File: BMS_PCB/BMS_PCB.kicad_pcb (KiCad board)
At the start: 2 copper layers, 168 parts, among them IC1 TPS560430XFDBVT, IC3 AMC1350DWVR, IC4 AMC1350DWVR, IC5 AMC1350DWVR, IC6 AMC1350DWVR, J1 Conn_01x37, J2 Conn_01x15, K1 J1021AS35VDC.20, Q1 2N7002KT7G, U1 TLV2404IDR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

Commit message: Bugfix Leiterbahn
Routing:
- net Net-(U3B--): track 28.5 -> 25.7 mm
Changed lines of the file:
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@@
-	)
-	(segment
-		(start 71.829501 136.4105)
-		(end 68.786503 136.4105)
-		(width 0.2)
-		(layer "F.Cu")
-		(net 31)
 	)
 	(segment
@@
 	)
 	(segment
-		(start 78.798 136.4105)
-		(end 64.779501 136.4105)
+		(start 64.421251 136.76875)
+		(end 61.516001 139.674)
 		(width 0.2)
 		(layer "F.Cu")
@@
 	)
 	(segment
-		(start 64.779501 136.4105)
-		(end 61.516001 139.674)
+		(start 79.15625 136.76875)
+		(end 79.15625 137.14375)
 		(width 0.2)
 		(layer "F.Cu")
@@
 	(segment
 		(start 79.15625 136.76875)
-		(end 79.15625 137.14375)
+		(end 64.421251 136.76875)
 		(width 0.2)
 		(layer "F.Cu")

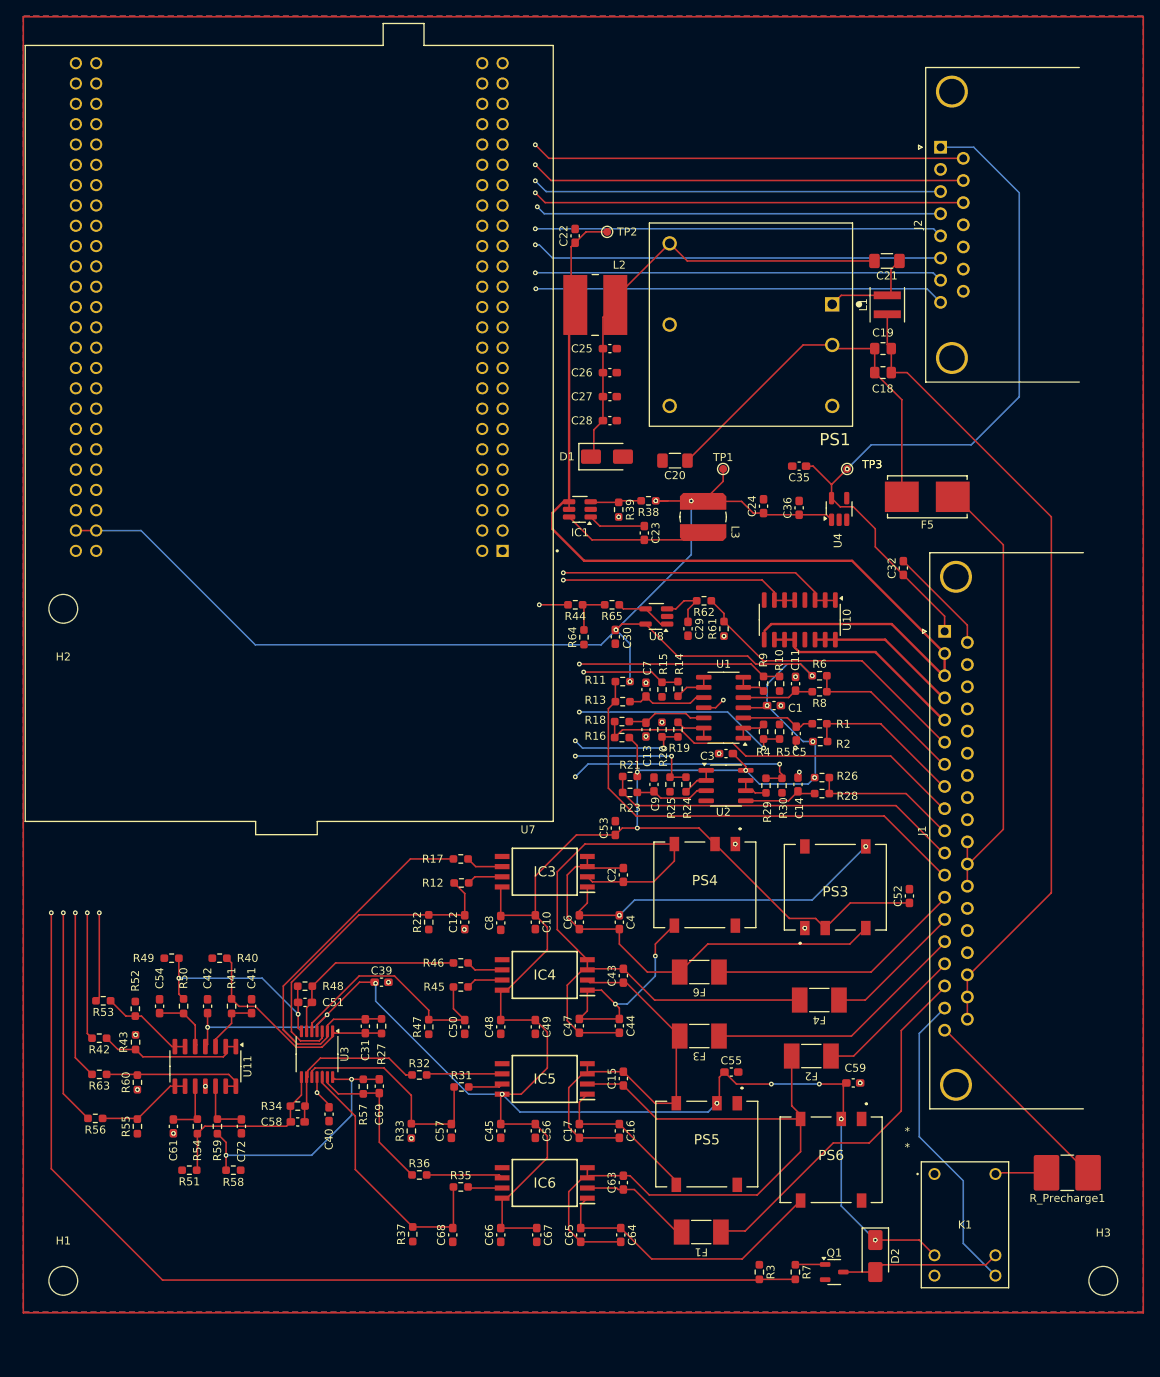
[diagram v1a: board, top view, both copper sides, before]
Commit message: Edge Cut hinzugefügt
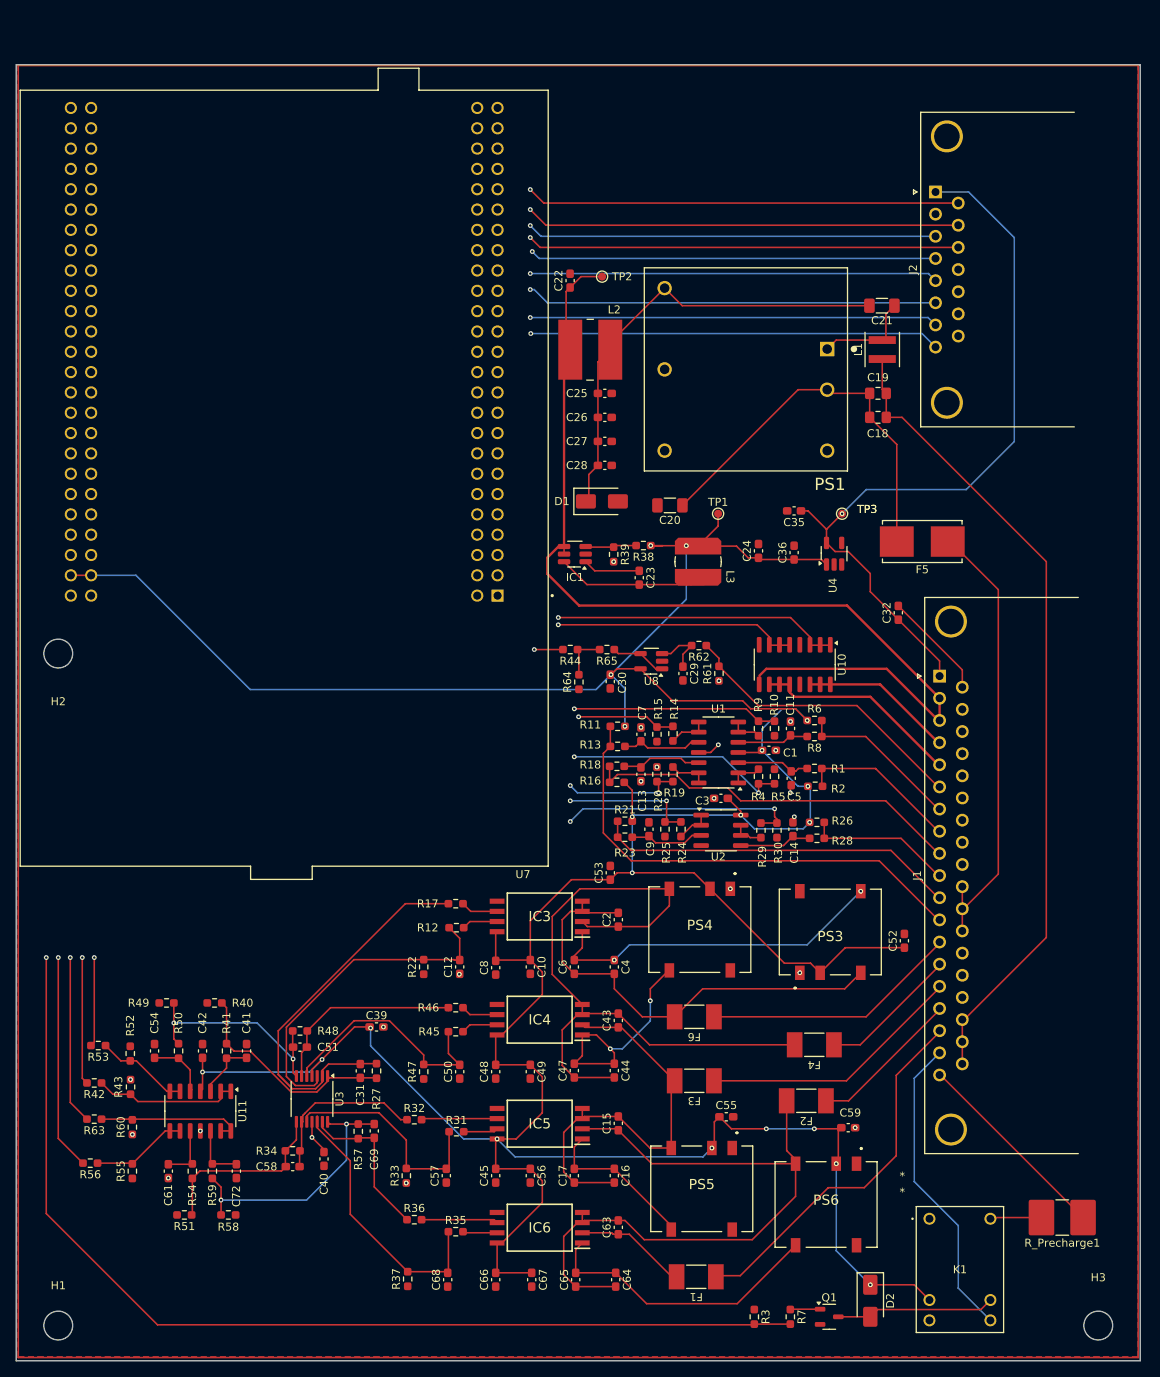
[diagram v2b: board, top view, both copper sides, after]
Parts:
- moved C2 5.63 mm to (99.8, 131.4)
- moved IC3 5.63 mm to (89.9, 131.0)
- moved R12 5.63 mm to (79.5, 132.4)
- moved R17 5.63 mm to (79.4, 129.4)
- moved C25 5.63 mm to (98.1, 65.6)
- moved C26 5.63 mm to (98.1, 68.6)
- moved C32 5.63 mm to (134.8, 93.0)
- moved D2 5.63 mm to (131.3, 179.0)
- moved C11 5.63 mm to (121.3, 107.5)
- moved C22 5.63 mm to (93.7, 51.5)
- moved C23 5.63 mm to (102.4, 88.6)
- moved C24 5.63 mm to (117.3, 85.3)
- moved C30 5.63 mm to (98.8, 101.6)
- moved C35 5.63 mm to (121.7, 80.3)
- moved C36 5.63 mm to (121.7, 85.5)
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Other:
- board outline added: 140.5 x 162 mm

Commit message: few changes
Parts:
- removed C32: 0,1uF, Capacitor_SMD:C_0603_1608Metric_Pad1.08x0.95mm_HandSolder
- removed H1, H2, H3: MountingHole_3.6mm, MountingHole:MountingHole_3.7mm
- added C33: 0,1uF, Resistor_SMD:R_0603_1608Metric_Pad0.98x0.95mm_HandSolder, F.Cu at (132.9, 91.0)
- C52, C53, C55, C59: footprint Capacitor_SMD:C_0603_1608Metric_Pad1.08x0.95mm_HandSolder -> Resistor_SMD:R_1206_3216Metric_Pad1.30x1.75mm_HandSolder
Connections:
- net Display_CLK renamed Display_SCK
- net Vcc_Current renamed +3.3V
- C22 pad 1: Relais_in+ -> +12V
- IC1 pad 4: Relais_in+ -> +12V
- IC1 pad 5: Relais_in+ -> +12V
- J1 pad 2: Relais_in+ -> Relais_in-
- J1 pad 4: Relais_out+ -> +12V
- J1 pad 5: Relais_out- -> +12V
- J2 pad 6: Display_D/C -> Display_DC
- K1 pad 1: (no net) -> unconnected-(K1-Pad1)
- L2 pad 2: Relais_in+ -> +12V
- TP2 pad 1: Relais_in+ -> +12V
- U10 pad 1: Relais_uC -> Relais+_uC
- U10 pad 10: Relais_out- -> Relais_in-
- U10 pad 11: Relais_out- -> Relais_in-
- U10 pad 12: Relais_out- -> Relais_in-
- U10 pad 14: Relais_out+ -> Relais_in+
- U10 pad 15: Relais_out+ -> Relais_in+
- U10 pad 16: Relais_out+ -> Relais_in+
- U10 pad 2: Relais_uC -> Relais+_uC
- U10 pad 3: Relais_uC -> Relais+_uC
- U10 pad 5: Relais_uC -> Relais-_uC
- U10 pad 6: Relais_uC -> Relais-_uC
- U10 pad 7: Relais_uC -> Relais-_uC
- U10 pad 9: Relais_in+ -> +12V
- U7 pad P1_10: Temp4_uC -> Touchdisplay_x
- U7 pad P1_11: Voltage01_uC -> Current_uC
- U7 pad P1_13: Voltage23_uC -> Voltage12_uC
- U7 pad P1_14: Voltage12_uC -> Voltage01_uC
- U7 pad P1_16: Temp6_uC -> Voltage23_uC
- U7 pad P1_17: Display_MOSI -> Temp1_uC
- U7 pad P1_18: Touchdisplay_x -> Voltage34_uC
- U7 pad P1_19: Temp3_uC -> Temp6_uC
- U7 pad P1_20: Voltage34_uC -> Temp5_uC
- U7 pad P1_21: Temp2_uC -> Temp3_uC
- U7 pad P1_22: Temp1_uC -> Temp2_uC
- U7 pad P1_7: Current_uC -> Temp4_uC
- U7 pad P1_8: Touchdisplay_y -> unconnected-(U7A-PC0-PadP1_8)
- U7 pad P1_9: Temp5_uC -> Touchdisplay_y
- U7 pad P2_23: Display_CS -> unconnected-(U7B-PB6-PadP2_23)
- U7 pad P2_24: Display_D/C -> unconnected-(U7B-PB7-PadP2_24)
- U7 pad P2_26: unconnected-(U7B-PB5-PadP2_26) -> Display_MOSI
- U7 pad P2_27: unconnected-(U7B-PD7-PadP2_27) -> Display_DC
- U7 pad P2_30: unconnected-(U7B-PD6-PadP2_30) -> Display_CS
- U7 pad P2_31: unconnected-(U7B-PD3-PadP2_31) -> Display_RST
- U7 pad P2_33: Relais_uC -> Relais+_uC
- U7 pad P2_34: Display_RST -> Relais-_uC
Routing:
- net Relais_uC: track 66.5 -> 0.00 mm, vias 2 -> 0
- net Display_D/C: track 51.3 -> 0.00 mm, vias 1 -> 0
- net Display_DC: track 0.00 -> 51.3 mm
- net Relais+_uC: track 0.00 -> 36.0 mm, vias 0 -> 1
- net Relais-_uC: track 0.00 -> 30.5 mm, vias 0 -> 1
- net Relais_out-: track 26.4 -> 0.00 mm
- net (no net): track 0.00 -> 26.4 mm
- net Relais_in+: track 127.6 -> 147.2 mm
- net Relais_out+: track 19.6 -> 0.00 mm
- net unconnected-(U7B-PB7-PadP2_24): vias 0 -> 1

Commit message: Freilaufdiode
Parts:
- added D3: 1N4007, Diode_SMD:D_SMA, F.Cu at (113.0, 29.4)
- added D4: 1N4007, Diode_SMD:D_SMA, F.Cu at (113.0, 34.0)
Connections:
- J1 pad 3: Relais_in+ -> +12V
- J1 pad 4: +12V -> Relais_in+

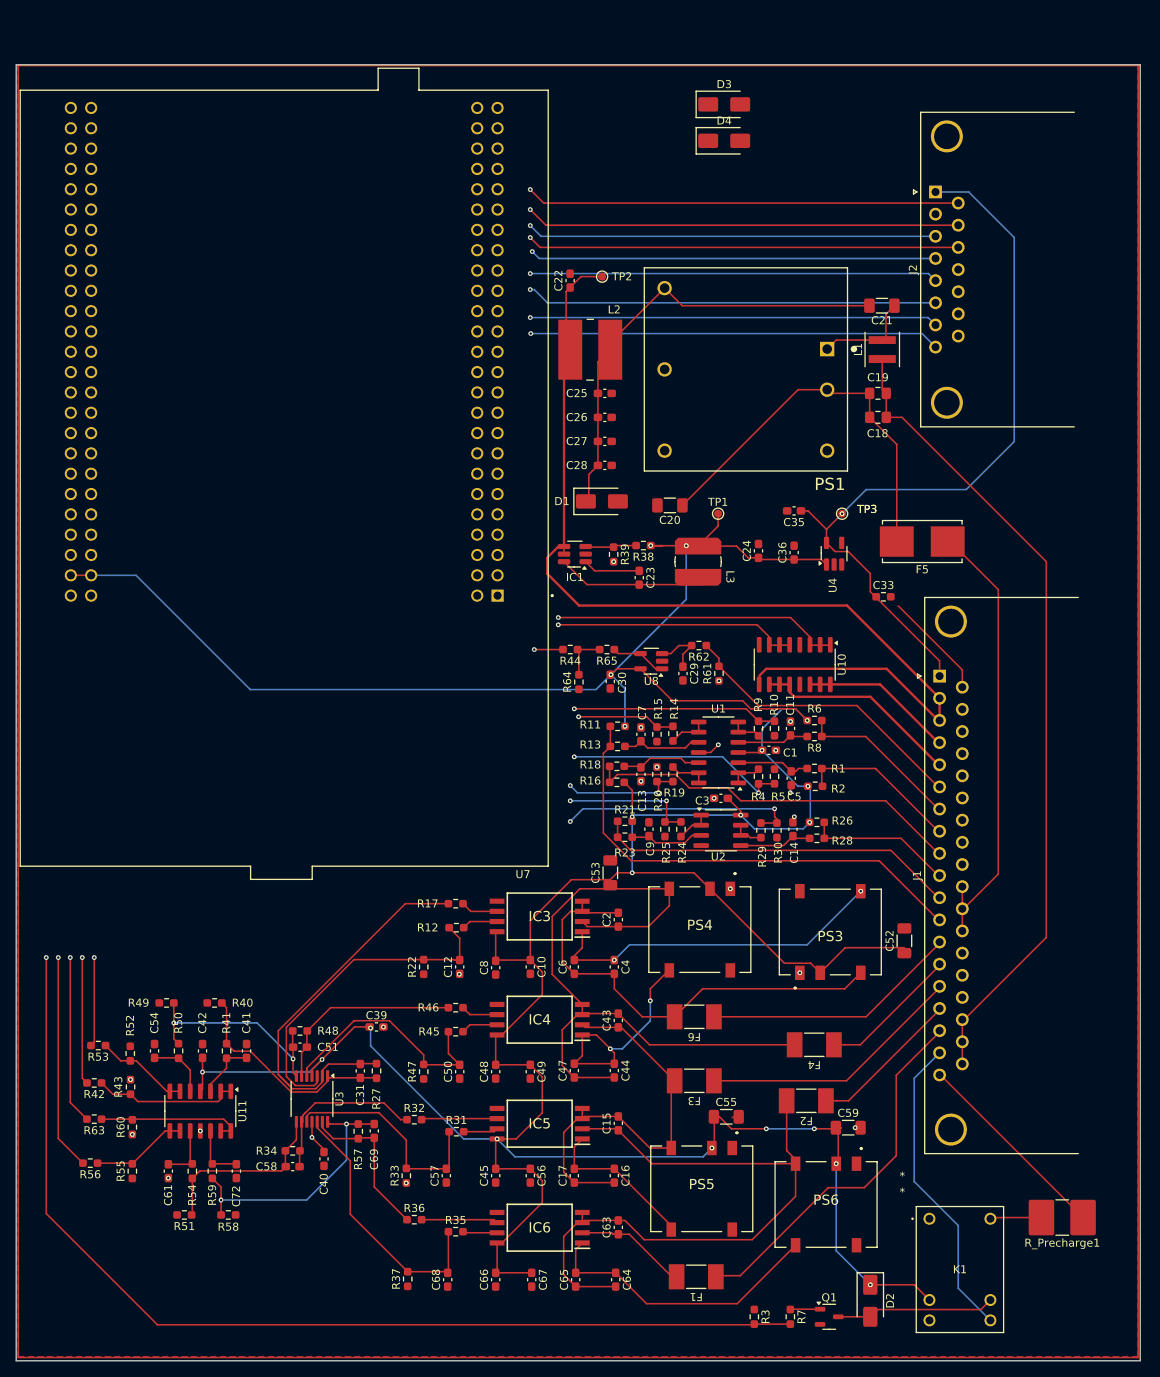
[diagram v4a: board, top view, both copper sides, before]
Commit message: Sonntag, 04.05.
Leiterbahndicken angepasst, Bohrlöcher erneuert, µC final angeschlossen, letzte Bugfixes
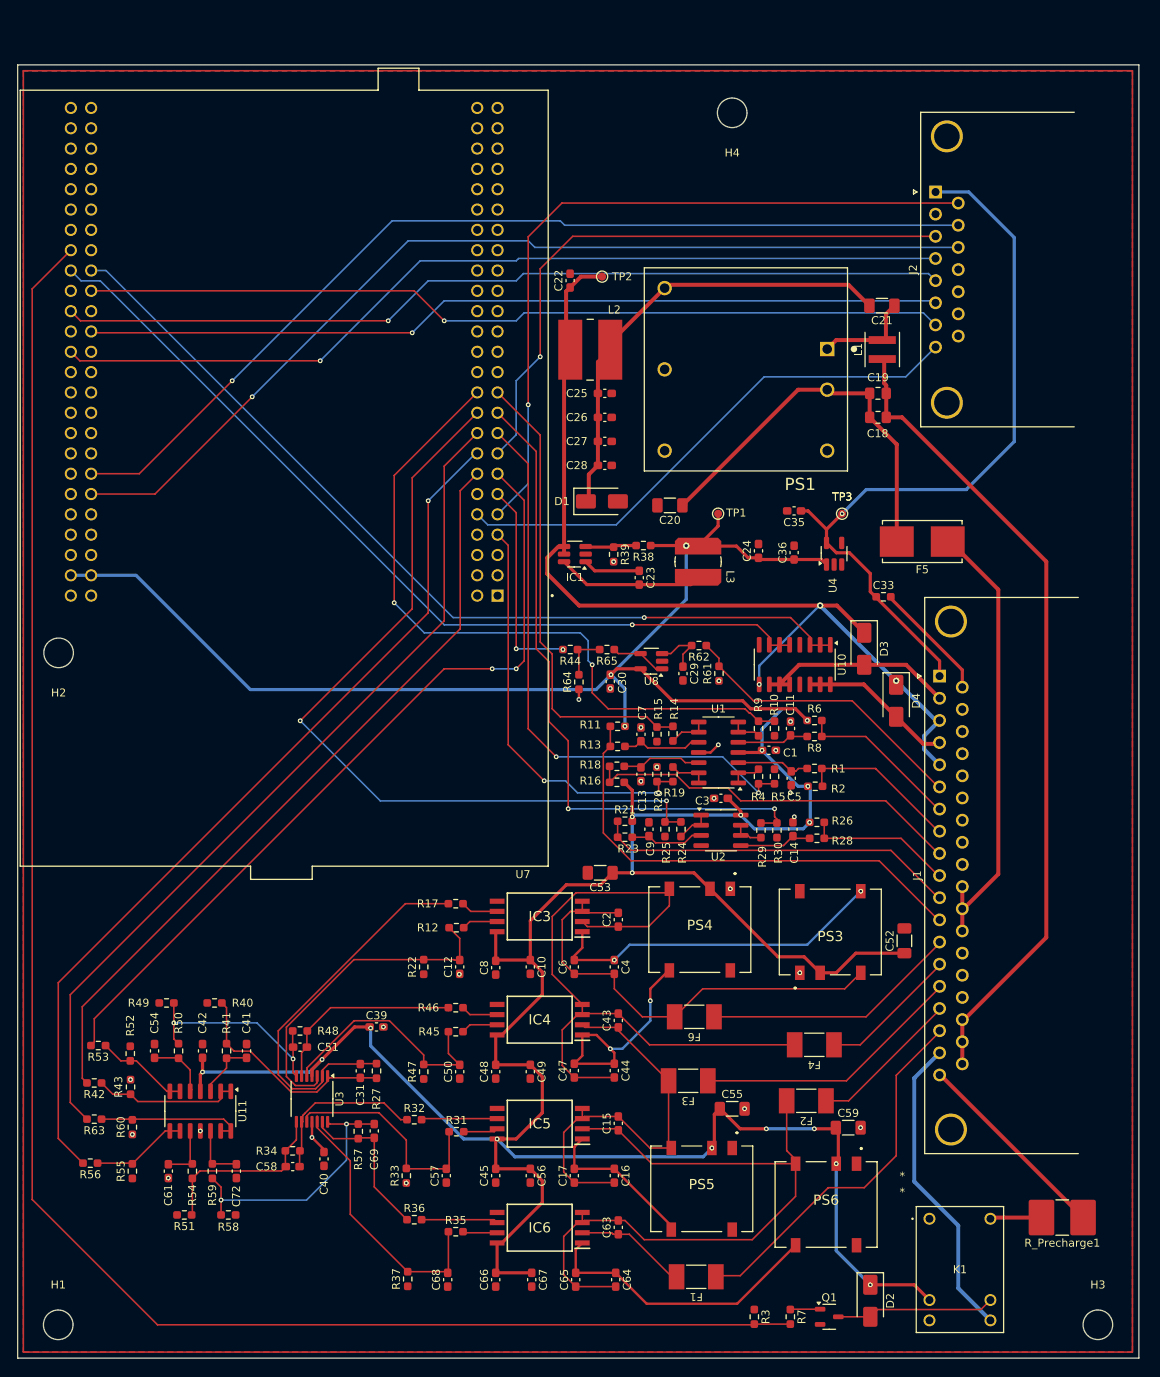
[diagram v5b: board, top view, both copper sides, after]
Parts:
- added H1: MountingHole_3.6mm, MountingHole:MountingHole_3.7mm, F.Cu at (29.8, 182.0)
- added H2: MountingHole_3.6mm, MountingHole:MountingHole_3.7mm, F.Cu at (29.8, 98.0)
- added H3: MountingHole_3.6mm, MountingHole:MountingHole_3.7mm, F.Cu at (159.7, 182.0)
- added H4: MountingHole_3.6mm, MountingHole:MountingHole_3.7mm, F.Cu at (114.0, 30.5)
- moved D4 73.2 mm to (134.5, 104.0), turned to -90 degrees
- moved D3 70.3 mm to (130.5, 97.5), turned to -90 degrees
- moved C53 1.26 mm to (97.5, 125.5), turned to 180 degrees
- moved C55 1.24 mm to (114.0, 155.0)
- moved F3 0.76 mm to (108.5, 151.5)
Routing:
- net Relais_in+: track 147.2 -> 19.6 mm
- net +12V: track 0.00 -> 126.2 mm, vias 0 -> 3
- net Precharge_uC: track 130.8 -> 222.0 mm, vias 1 -> 0
- net Voltage12_uC: track 11.2 -> 100.6 mm, vias 1 -> 2
- net Voltage34_uC: track 21.1 -> 107.7 mm, vias 1 -> 0
- net Temp5_uC: track 16.8 -> 102.3 mm
- net Voltage23_uC: track 27.0 -> 111.8 mm
- net Voltage01_uC: track 15.9 -> 96.8 mm, vias 1 -> 0
- net Relais-_uC: track 30.5 -> 109.8 mm
- net Relais+_uC: track 36.0 -> 112.3 mm
- net Touchdisplay_y-: track 54.0 -> 121.8 mm
- net Touchdisplay_x-: track 54.3 -> 121.7 mm
- net Display_MOSI: track 50.8 -> 113.9 mm
- net Temp2_uC: track 25.7 -> 87.8 mm, vias 1 -> 2
- net Display_CS: track 51.0 -> 111.4 mm
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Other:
- board size 140.5 x 162 mm -> 140.2 x 161.7 mm
